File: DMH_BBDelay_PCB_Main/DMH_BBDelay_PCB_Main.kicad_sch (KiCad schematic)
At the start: 7 parts, among them J100 IDC_02x08, J9 Conn_01x01

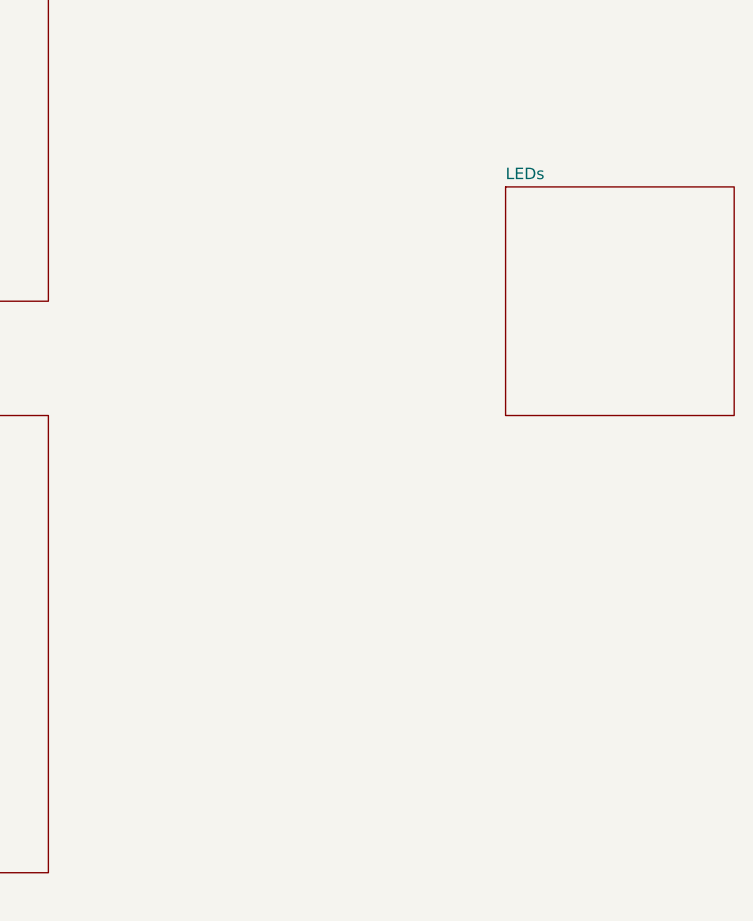
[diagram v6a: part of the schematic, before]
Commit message: Synced channel A and B schematics
... and applied several minor improvements and optimizations.
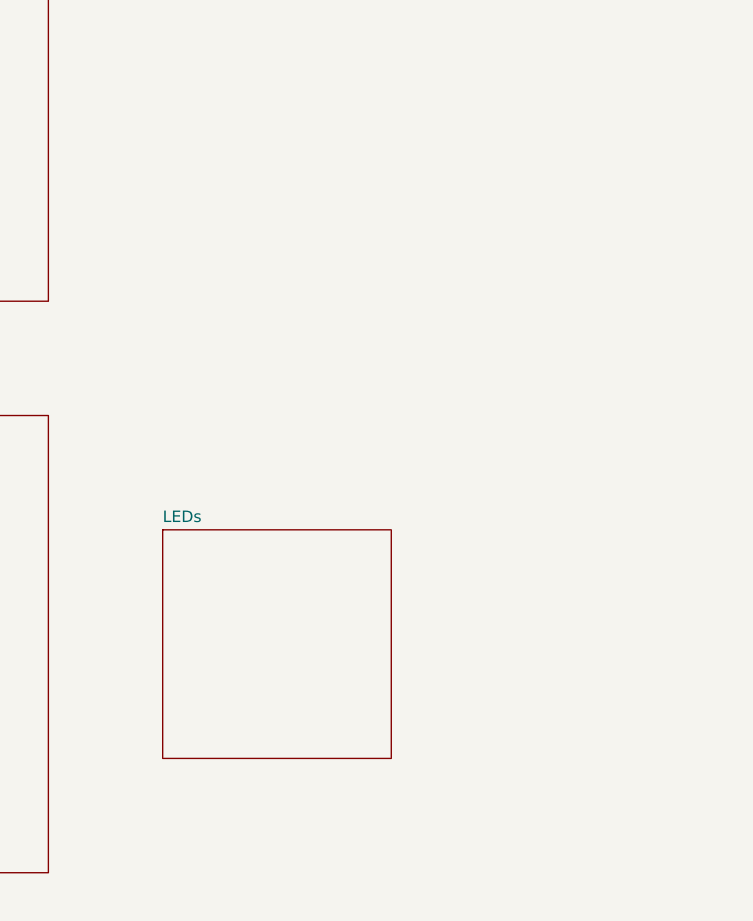
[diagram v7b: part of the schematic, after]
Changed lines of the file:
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@@
 	)
 	(sheet
-		(at 165.1 63.5)
+		(at 127 101.6)
 		(size 25.4 25.4)
 		(exclude_from_sim no)
@@
 		)
 		(property "Sheetname" "LEDs"
-			(at 165.1 62.7884 0)
+			(at 127 100.8884 0)
 			(show_name no)
 			(do_not_autoplace no)
@@
 		)
 		(property "Sheetfile" "LEDs.kicad_sch"
-			(at 165.1 89.4846 0)
+			(at 127 127.5846 0)
 			(hide yes)
 			(show_name no)
